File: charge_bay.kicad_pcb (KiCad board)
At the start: 4 copper layers, 90 x 51.4 mm, 111 parts, among them J1 USB_C_Receptacle_USB2.0, J10 Conn_01x03_Pin, J11 Conn_01x05_Socket, J2 Screw_Terminal_01x04, J3 Conn_01x03_Pin, J4 Conn_01x03_Pin, J5 Conn_01x03_Pin, J6 Conn_01x05_Socket, J7 Screw_Terminal_01x04, J8 Conn_01x03_Pin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

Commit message: Adjustments for Generation
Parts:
- moved C1 109.4 mm to (30.2, 59.6)
- moved C10 109.4 mm to (31.5, 62.2)
- moved C12 109.4 mm to (31.4, 55.1)
- moved C13 109.4 mm to (28.6, 51.7)
- moved C15 109.4 mm to (43.7, 63.3)
- moved C16 109.4 mm to (39.4, 56.1)
- moved C17 109.4 mm to (35.4, 57.6)
- moved C19 109.4 mm to (30.7, 66.8)
- moved C2 109.4 mm to (30.2, 60.8)
- moved C3 109.4 mm to (48.7, 27.3)
- moved C4 109.4 mm to (48.7, 21.2)
- moved C5 109.4 mm to (29.7, 20.2)
- moved C6 109.4 mm to (29.8, 25.3)
- moved D1 109.4 mm to (36.1, 35.8)
- moved D2 109.4 mm to (36.1, 41.0)
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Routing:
- net (no net): vias 0 -> 1

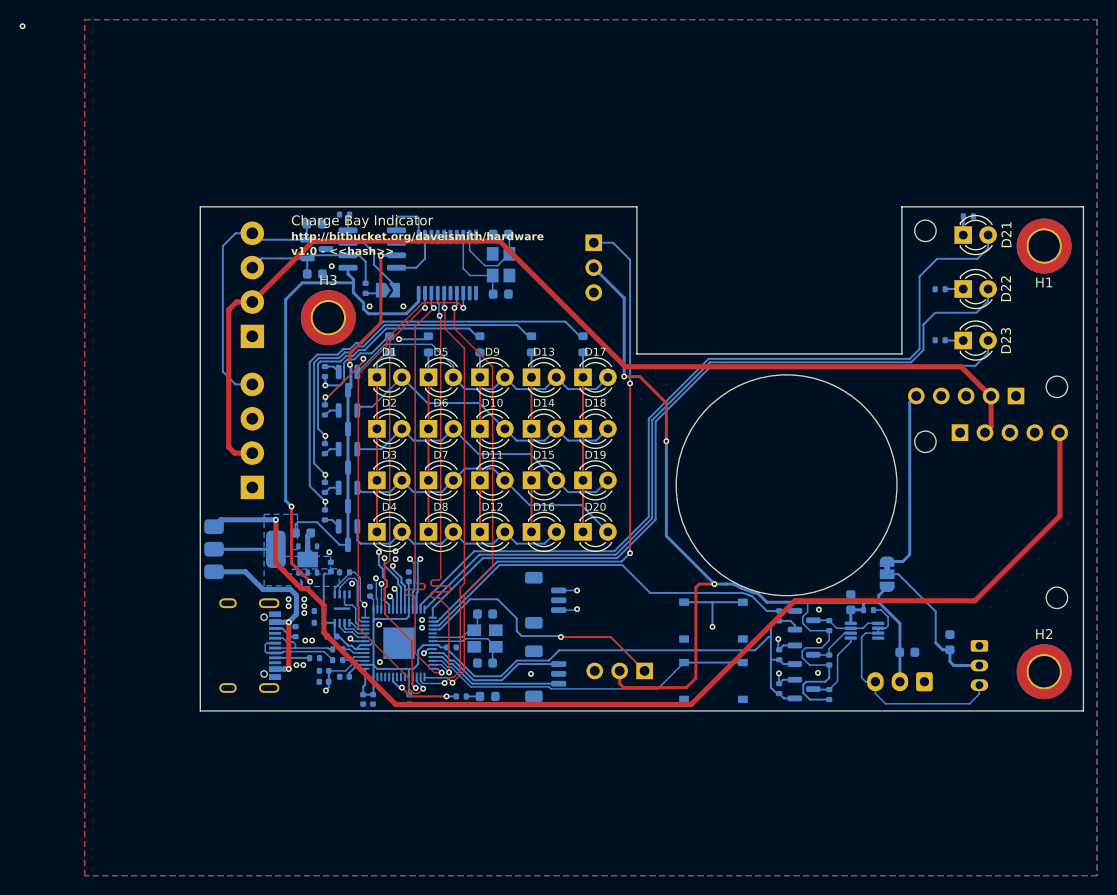
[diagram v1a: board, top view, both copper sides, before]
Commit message: Update Silkscreen With Pololu Parts
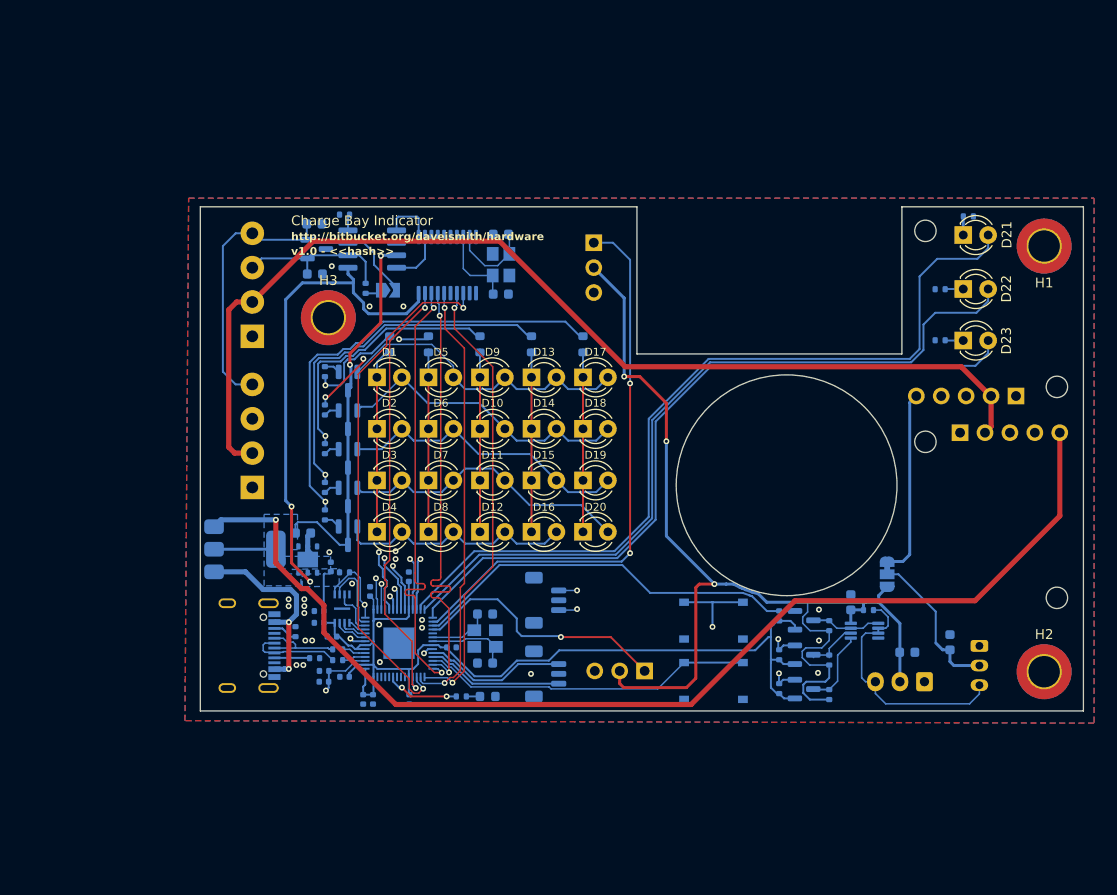
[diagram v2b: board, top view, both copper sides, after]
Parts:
- moved J1 0.07 mm to (21.9, 63.1)
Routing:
- net (no net): vias 1 -> 0
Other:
- board text added: "Pololu D24V50F5 +5V Regulator"
- board text added: "Pololu D36V28F7 +7.5V Regulator"
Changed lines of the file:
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@@
 		(tags "resistor")
 		(property "Reference" "R16"
-			(at 0 1.17 0)
+			(at -2.1894 0.047475 0)
 			(layer "B.SilkS")
 			(effects
@@
 		(tags "resistor")
 		(property "Reference" "R17"
-			(at 0 1.17 0)
+			(at -2.1894 0.072475 0)
 			(layer "B.SilkS")
 			(effects
@@
 		(tags "resistor")
 		(property "Reference" "R15"
-			(at -1.6 0 90)
+			(at -2.1106 -0.047475 180)
 			(layer "B.SilkS")
 			(effects
@@
 	(footprint "Connector_USB:USB_C_Receptacle_G-Switch_GT-USB-7010ASV"
 		(layer "B.Cu")
-		(at 22.0094 63.122525 90)
+		(at 21.94 63.122525 90)
 		(descr "USB Type C, right-angle, SMT, https://datasheet.lcsc.com/lcsc/2204071530_G-Switch-GT-USB-7010ASV_C2988369.pdf")
 		(tags "USB C Type-C Receptacle SMD")
@@
 		(layer "Edge.Cuts")
 	)
+	(gr_text "Pololu D24V50F5\n+5V Regulator"
+		(at 104.225 45.675 0)
+		(layer "B.SilkS")
+		(effects
+			(font
+				(size 0.8 0.8)
+				(thickness 0.15)
+				(bold yes)
+			)
+			(justify left bottom mirror)
+		)
+	)
 	(gr_text "SIG"
 		(at 56.4644 22.052525 0)
@@
 		)
 	)
+	(gr_text "Pololu D36V28F7\n+7.5V Regulator"
+		(at 100.5 35.8 0)
+		(layer "B.SilkS")
+		(effects
+			(font
+				(size 0.8 0.8)
+				(thickness 0.15)
+				(bold yes)
+			)
+			(justify left bottom mirror)
+		)
+	)
 	(gr_text "http://bitbucket.org/daveismith/hardware"
 		(at 27.3644 21.902525 0)
@@
 	)
 	(via
-		(at 0 0)
-		(size 0.6)
-		(drill 0.3)
-		(layers "F.Cu" "B.Cu")
-		(net 0)
-	)
-	(via
 		(at 81.1644 62.602525)
 		(size 0.6)
@@
 	)
 	(segment
-		(start 30.7358 63.733925)
-		(end 26.603 63.733925)
-		(width 0.1582)
-		(layer "B.Cu")
-		(net 16)
-	)
-	(segment
-		(start 24.8998 63.872525)
-		(end 25.7344 63.872525)
-		(width 0.1582)
-		(layer "B.Cu")
-		(net 16)
-	)
-	(segment
-		(start 26.4473 63.872525)
-		(end 25.7344 63.872525)
-		(width 0.1582)
-		(layer "B.Cu")
-		(net 16)
-	)
-	(segment
-		(start 24.8998 62.872525)
-		(end 24.7344 63.037925)
+		(start 25.7344 62.872525)
+		(end 24.702475 62.872525)
 		(width 0.1582)
 		(layer "B.Cu")
@@
 	)
 	(segment
-		(start 26.603 63.733925)
-		(end 26.5859 63.751025)
+		(start 26.5321 63.804825)
+		(end 26.603 63.733925)
 		(width 0.1582)
 		(layer "B.Cu")
@@
 	)
 	(segment
-		(start 24.7344 63.707125)
-		(end 24.8998 63.872525)
+		(start 24.525 63.05)
+		(end 24.525 63.625)
 		(width 0.1582)
 		(layer "B.Cu")
@@
 	)
 	(segment
-		(start 26.5859 63.751025)
-		(end 26.5859 63.733925)
+		(start 24.525 63.625)
+		(end 24.704825 63.804825)
 		(width 0.1582)
 		(layer "B.Cu")
@@
 	)
 	(segment
-		(start 24.7344 63.037925)
-		(end 24.7344 63.707125)
+		(start 30.7358 63.733925)
+		(end 31.6044 64.602525)
 		(width 0.1582)
 		(layer "B.Cu")
@@
 	)
 	(segment
-		(start 31.6044 64.602525)
+		(start 26.603 63.733925)
 		(end 30.7358 63.733925)
 		(width 0.1582)
@@
 	)
 	(segment
-		(start 26.5859 63.733925)
-		(end 26.4473 63.872525)
+		(start 24.704825 63.804825)
+		(end 26.5321 63.804825)
 		(width 0.1582)
 		(layer "B.Cu")
@@
 	)
 	(segment
-		(start 25.7344 62.872525)
-		(end 24.8998 62.872525)
+		(start 24.702475 62.872525)
+		(end 24.525 63.05)
 		(width 0.1582)
 		(layer "B.Cu")
@@
 		(polygon
 			(pts
-				(xy 109.525 86.575) (xy 6.321625 86.575) (xy 6.321625 -0.674) (xy 109.525 -0.674)
+				(xy 109.2 71.025) (xy 16.55 70.775) (xy 16.925 17.525) (xy 109.2 17.525)
 			)
 		)

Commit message: Update Silkscreen With Pololu Parts, etc.
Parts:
- C7, C8: value 15pF -> 30pF
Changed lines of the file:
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@@
 			)
 		)
-		(property "JLCPCB" "C111113"
+		(property "JLCPCB" "C20526"
 			(at 0 0 -90)
 			(unlocked yes)
@@
 			)
 		)
-		(property "JLCType" "Extended"
+		(property "JLCType" "Basic"
 			(at 0 0 -90)
 			(unlocked yes)
@@
 			)
 		)
-		(property "Value" "15pF"
+		(property "Value" "30pF"
 			(at 0 -1.43 0)
 			(layer "B.Fab")
@@
 			)
 		)
-		(property "JLCPCB" "C1644"
+		(property "JLCPCB" "C1658"
 			(at 0 0 180)
 			(unlocked yes)
@@
 			)
 		)
+		(property "JLCPCB" "C2876186"
+			(at 0 0 -90)
+			(unlocked yes)
+			(layer "B.Fab")
+			(hide yes)
+			(effects
+				(font
+					(size 1 1)
+					(thickness 0.15)
+				)
+				(justify mirror)
+			)
+		)
+		(property "JLCType" "Extended"
+			(at 0 0 -90)
+			(unlocked yes)
+			(layer "B.Fab")
+			(hide yes)
+			(effects
+				(font
+					(size 1 1)
+					(thickness 0.15)
+				)
+				(justify mirror)
+			)
+		)
 		(property ki_fp_filters "WSON*1EP*3x3mm*P0.95mm*")
 		(sheetname "Root")
@@
 		)
 		(property "Value" "Conn_01x05_Socket"
-			(at 0 -12.93 90)
+			(at 5.427475 -4.2056 180)
 			(layer "B.Fab")
 			(effects
@@
 			)
 		)
-		(property "JLCPCB" "C111113"
+		(property "JLCPCB" "C20526"
 			(at 0 0 -90)
 			(unlocked yes)
@@
 			)
 		)
-		(property "JLCType" "Extended"
+		(property "JLCType" "Basic"
 			(at 0 0 -90)
 			(unlocked yes)
@@
 			)
 		)
-		(property "JLCPCB" "C111113"
+		(property "JLCPCB" "C20526"
 			(at 0 0 -90)
 			(unlocked yes)
@@
 			)
 		)
-		(property "JLCType" "Extended"
+		(property "JLCType" "Basic"
 			(at 0 0 -90)
 			(unlocked yes)
@@
 			)
 		)
-		(property "JLCPCB" "C111113"
+		(property "JLCPCB" "C20526"
 			(at 0 0 -90)
 			(unlocked yes)
@@
 			)
 		)
-		(property "JLCType" "Extended"
+		(property "JLCType" "Basic"
 			(at 0 0 -90)
 			(unlocked yes)
@@
 			)
 		)
-		(property "JLCPCB" "C111113"
+		(property "JLCPCB" "C20526"
 			(at 0 0 -90)
 			(unlocked yes)
@@
 			)
 		)
-		(property "JLCType" "Extended"
+		(property "JLCType" "Basic"
 			(at 0 0 -90)
 			(unlocked yes)
@@
 			)
 		)
-		(property "Value" "15pF"
+		(property "Value" "30pF"
 			(at 0 -1.43 180)
 			(layer "B.Fab")
@@
 			)
 		)
-		(property "JLCPCB" "C1644"
+		(property "JLCPCB" "C1658"
 			(at 0 0 0)
 			(unlocked yes)
@@
 			)
 		)
-		(property "Datasheet" ""
+		(property "Datasheet" "https://jlcpcb.com/partdetail/Yxc_CrystalOscillators-X322512MSB4SI/C9002"
 			(at 0 0 180)
 			(unlocked yes)
@@
 			)
 		)
-		(property "JLCPCB" "C20625731"
+		(property "JLCPCB" "C9002"
 			(at 0 0 0)
 			(unlocked yes)
@@
 			)
 		)
-		(property "JLCType" "Extended"
+		(property "JLCType" "Basic"
 			(at 0 0 0)
 			(unlocked yes)
@@
 		)
 	)
-	(gr_rect
-		(start 89.8144 40.152525)
+	(gr_line
+		(start 103.1 38.95)
+		(end 107.6144 38.952525)
+		(stroke
+			(width 0.1)
+			(type default)
+		)
+		(layer "B.SilkS")
+	)
+	(gr_line
+		(start 89.8144 60.452525)
 		(end 107.6144 60.452525)
 		(stroke
@@
 			(type default)
 		)
-		(fill none)
+		(layer "B.SilkS")
+	)
+	(gr_line
+		(start 107.6144 38.952525)
+		(end 107.6144 18.652525)
+		(stroke
+			(width 0.1)
+			(type default)
+		)
 		(layer "B.SilkS")
 	)
@@
 		(layer "B.SilkS")
 	)
-	(gr_rect
-		(start 107.6144 38.952525)
-		(end 89.8144 18.652525)
+	(gr_line
+		(start 89.8144 40.152525)
+		(end 93.75 40.15)
 		(stroke
 			(width 0.1)
 			(type default)
 		)
-		(fill none)
 		(layer "B.SilkS")
 	)
@@
 	)
 	(gr_line
+		(start 89.8144 40.152525)
+		(end 89.8144 60.452525)
+		(stroke
+			(width 0.1)
+			(type default)
+		)
+		(layer "B.SilkS")
+	)
+	(gr_line
+		(start 89.8144 18.652525)
+		(end 89.8144 36.15)
+		(stroke
+			(width 0.1)
+			(type default)
+		)
+		(layer "B.SilkS")
+	)
+	(gr_line
+		(start 107.6144 18.652525)
+		(end 89.8144 18.652525)
+		(stroke
+			(width 0.1)
+			(type default)
+		)
+		(layer "B.SilkS")
+	)
+	(gr_line
 		(start 38.3644 67.352525)
 		(end 36.2644 67.352525)
@@
 	)
 	(gr_line
+		(start 93.75 40.15)
+		(end 89.8144 40.152525)
+		(stroke
+			(width 0.1)
+			(type default)
+		)
+		(layer "B.SilkS")
+	)
+	(gr_line
 		(start 36.2644 69.702525)
 		(end 38.3644 69.702525)
@@
 	)
 	(gr_line
+		(start 107.6144 60.452525)
+		(end 107.6144 43.175)
+		(stroke
+			(width 0.1)
+			(type default)
+		)
+		(layer "B.SilkS")
+	)
+	(gr_line
 		(start 31.4644 68.202525)
 		(end 31.9644 66.702525)
@@
 	)
 	(group ""
-		(members "01b51d6b-8ff0-4f9e-a073-4780a6e7700e" "6a1f04f3-37eb-4f9b-97d9-d0fe86aa8072"
-			"7151707b-5df2-4e9b-8991-87690529ac64" "d3f960e0-f35e-4ffc-adc7-ed5bc1af20be"
+		(members "1cae9be7-7fb1-4040-bfb5-a3eeab1f520b" "68d34644-0b2c-46d1-b79a-a672fc7c5704"
+			"6a1f04f3-37eb-4f9b-97d9-d0fe86aa8072" "7151707b-5df2-4e9b-8991-87690529ac64"
+			"7cbaecb7-b33c-433b-ba18-7f95e2510d09" "d3f960e0-f35e-4ffc-adc7-ed5bc1af20be"
+			"e1102198-d26e-48b8-a344-ce362a55cdb9" "f574cff3-2ba3-4409-bf88-3c1f7cb23154"
 		)
 	)
 	(group ""
-		(members "0372432a-7772-41ed-b8e3-ceab32187c84" "5ce26524-e1b0-4561-8143-816981e446b8"
-			"6a14aedb-5e4a-46b7-83e0-b0f86440ee7a" "87642d0c-c436-448f-8e76-8a97a52d072d"
-			"bce9b3cb-2215-46e0-ba66-8cb0782d6dcc" "f62766be-20ea-4dce-b4ba-a7a6b4853e1c"
+		(members "0372432a-7772-41ed-b8e3-ceab32187c84" "04be0617-17fd-4b20-8b2e-c0398d7231bf"
+			"2a5c024c-e443-431a-b764-d70a975b64ff" "6a14aedb-5e4a-46b7-83e0-b0f86440ee7a"
+			"87642d0c-c436-448f-8e76-8a97a52d072d" "88368c86-12d8-4477-847d-94752532f54d"
+			"8d3c252d-5422-4c7a-b87f-9efcd417ec84" "bce9b3cb-2215-46e0-ba66-8cb0782d6dcc"
+			"f62766be-20ea-4dce-b4ba-a7a6b4853e1c"
 		)
 	)
